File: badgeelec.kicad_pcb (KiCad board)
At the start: 2 copper layers, 60 x 60 mm, 29 parts, among them J1 PROG_CONN, U1 PIC16F716-I-SO-ND, U2 TSSP58038, Y1 4Mhz

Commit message: Cut revision 3
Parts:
- removed the G*** at (100.0, 90.0)
- added G***: LOGO, ext_libs:spade_bold, F.Cu at (100.0, 99.5)
- moved S1 7.00 mm to (100.0, 119.2)
- moved C3 5.70 mm to (93.2, 117.9)
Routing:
- net /~MCLR: track 67.4 -> 73.0 mm
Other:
- board text removed: "0x0G"

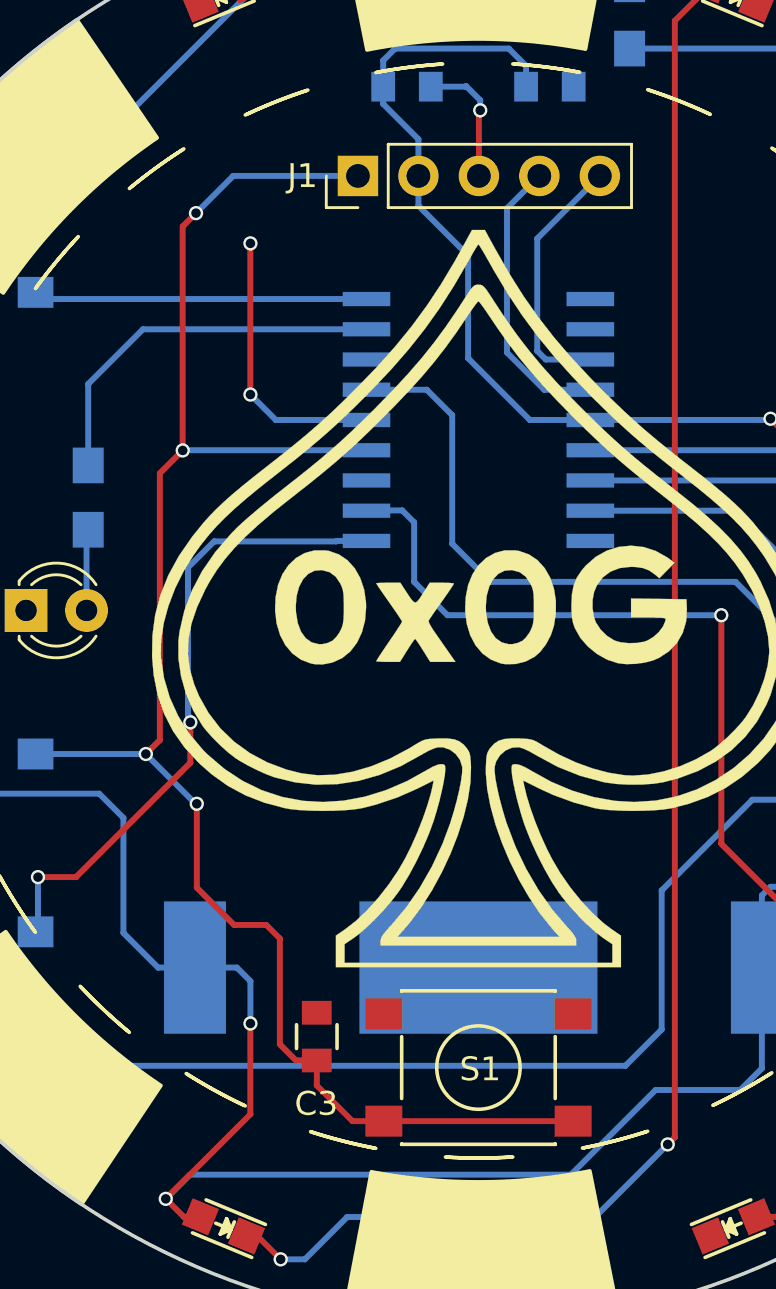
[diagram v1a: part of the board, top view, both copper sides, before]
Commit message: Cut r4
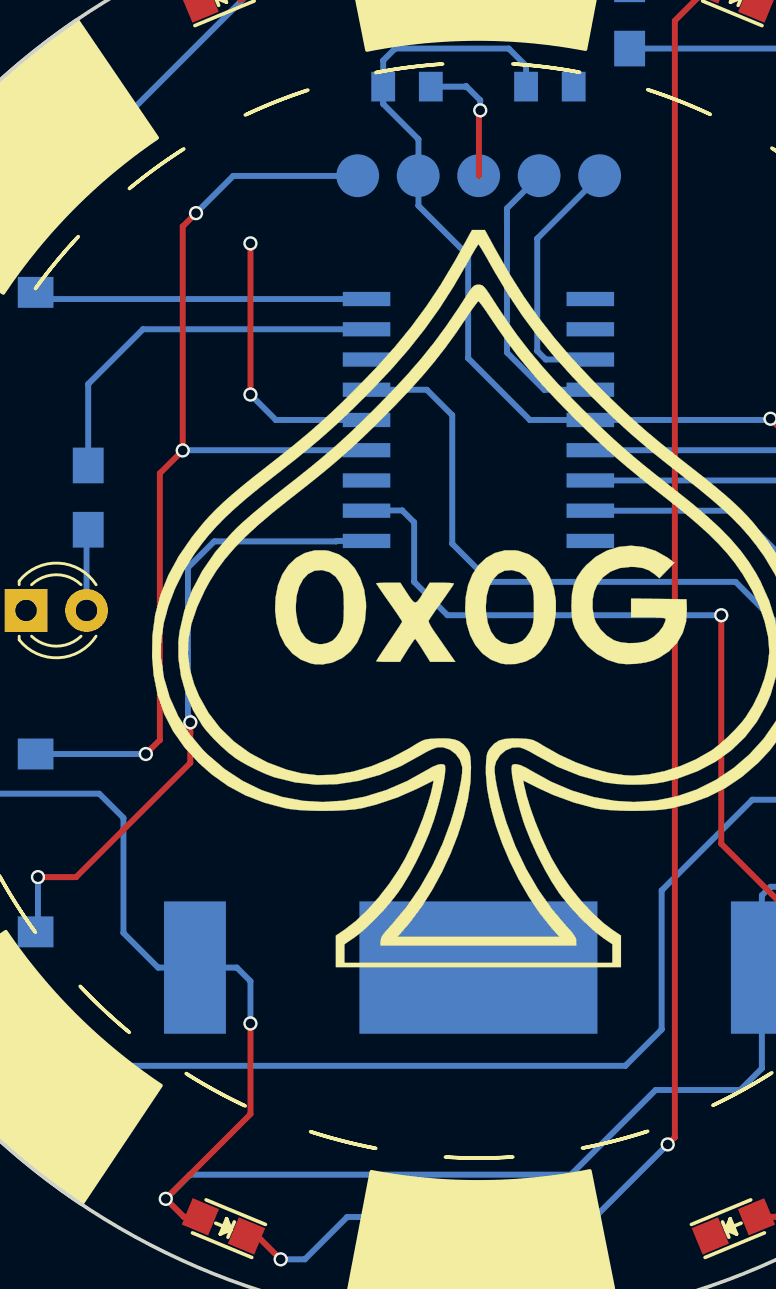
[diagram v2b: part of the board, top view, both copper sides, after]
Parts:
- removed C3: 10nF, Capacitors_SMD:C_0805
- removed S1: PTS645SM43SMTR92, Buttons_Switches_SMD:SW_SPST_PTS645
- J1: footprint Pin_Headers:Pin_Header_Straight_1x05_Pitch2.54mm -> ext_libs:SMD_PROG_5; moved to B.Cu
- moved J1 5.07 mm to (100.0, 81.7), turned to 0 degrees
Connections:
- U1 pad 10: (no net) -> /RB4
- U1 pad 11: (no net) -> /RB5
- U1 pad 18: (no net) -> /RA1
- U1 pad 3: (no net) -> Net-(U1-Pad3)
- U1 pad 7: (no net) -> /RB1
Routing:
- net /~MCLR: track 73.0 -> 43.4 mm, vias 4 -> 3

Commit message: First pass verifying everything
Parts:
- R1: value 220 -> 1k
- R2: value 220 -> 430
- R3, R4: value 150 -> 220
- R8: value 200R -> 220
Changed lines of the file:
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@@
   (title_block
     (title "0x0G Badge 2018")
-    (date 2018-05-03)
+    (date 2018-05-07)
     (rev r4)
     (company "Google LLC")
@@
       (effects (font (size 1 1) (thickness 0.15)) (justify mirror))
     )
-    (fp_text value 220 (at 0 -2.1 270) (layer B.Fab)
+    (fp_text value 1k (at 0 -2.1 270) (layer B.Fab)
       (effects (font (size 1 1) (thickness 0.15)) (justify mirror))
     )
@@
       (effects (font (size 1 1) (thickness 0.15)) (justify mirror))
     )
-    (fp_text value 220 (at 0 -2.1) (layer B.Fab)
+    (fp_text value 430 (at 0 -2.1) (layer B.Fab)
       (effects (font (size 1 1) (thickness 0.15)) (justify mirror))
     )
@@
       (effects (font (size 1 1) (thickness 0.15)) (justify mirror))
     )
-    (fp_text value 150 (at 0 -2.1) (layer B.Fab)
+    (fp_text value 220 (at 0 -2.1) (layer B.Fab)
       (effects (font (size 1 1) (thickness 0.15)) (justify mirror))
     )
@@
       (effects (font (size 1 1) (thickness 0.15)) (justify mirror))
     )
-    (fp_text value 150 (at 0 -2.1 180) (layer B.Fab)
+    (fp_text value 220 (at 0 -2.1 180) (layer B.Fab)
       (effects (font (size 1 1) (thickness 0.15)) (justify mirror))
     )
@@
       (effects (font (size 1 1) (thickness 0.15)) (justify mirror))
     )
-    (fp_text value 200R (at 0 -2.1 270) (layer B.Fab)
-      (effects (font (size 1 1) (thickness 0.15)) (justify mirror))
-    )
+    (fp_text value 220 (at 0 -2.1 270) (layer B.Fab)
+      (effects (font (size 1 1) (thickness 0.15)) (justify mirror))
+    )
